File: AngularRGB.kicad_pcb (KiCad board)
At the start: 2 copper layers, 228.6 x 76.2 mm, 114 parts, among them SW1 SW_Push, SW1.25U1 MX_1.25U, SW1.25U2 MX_1.25U, SW1.25U3 MX_1.25U, SW1.25U4 MX_1.25U, SW1.25U5 MX_1.25U, SW1.25U6 MX_1.25U, SW1.75U1 MX_1.75U, SW1.75U2 MX_1.75U, SW10 MX_1U, SW11 MX_1U, SW12 MX_1U, SW13 MX_1U, SW14 MX_1U, SW15 MX_1U, SW16 MX_1U, SW17 MX_1U, SW18 MX_1U, SW19 MX_1U, SW2 MX_1U, SW2.25U1 MX_2.25U, SW2.75U1 MX_2.75U, SW20 MX_1U, SW21 MX_1U, SW22 MX_1U, SW23 MX_1U, SW24 MX_1U, SW25 MX_1U, SW26 MX_1U, SW27 MX_1U, SW28 MX_1U, SW29 MX_1U, SW3 MX_1U, SW30 MX_1U, SW31 MX_1U, SW32 MX_1U, SW33 MX_1U, SW4 MX_1U, SW5 MX_1U, SW6 MX_1U, SW7 MX_1U, SW8 MX_1U, SW9 MX_1U, U1 ATmega32U4-MU, U2 USB6B1, Y1 Crystal_GND24

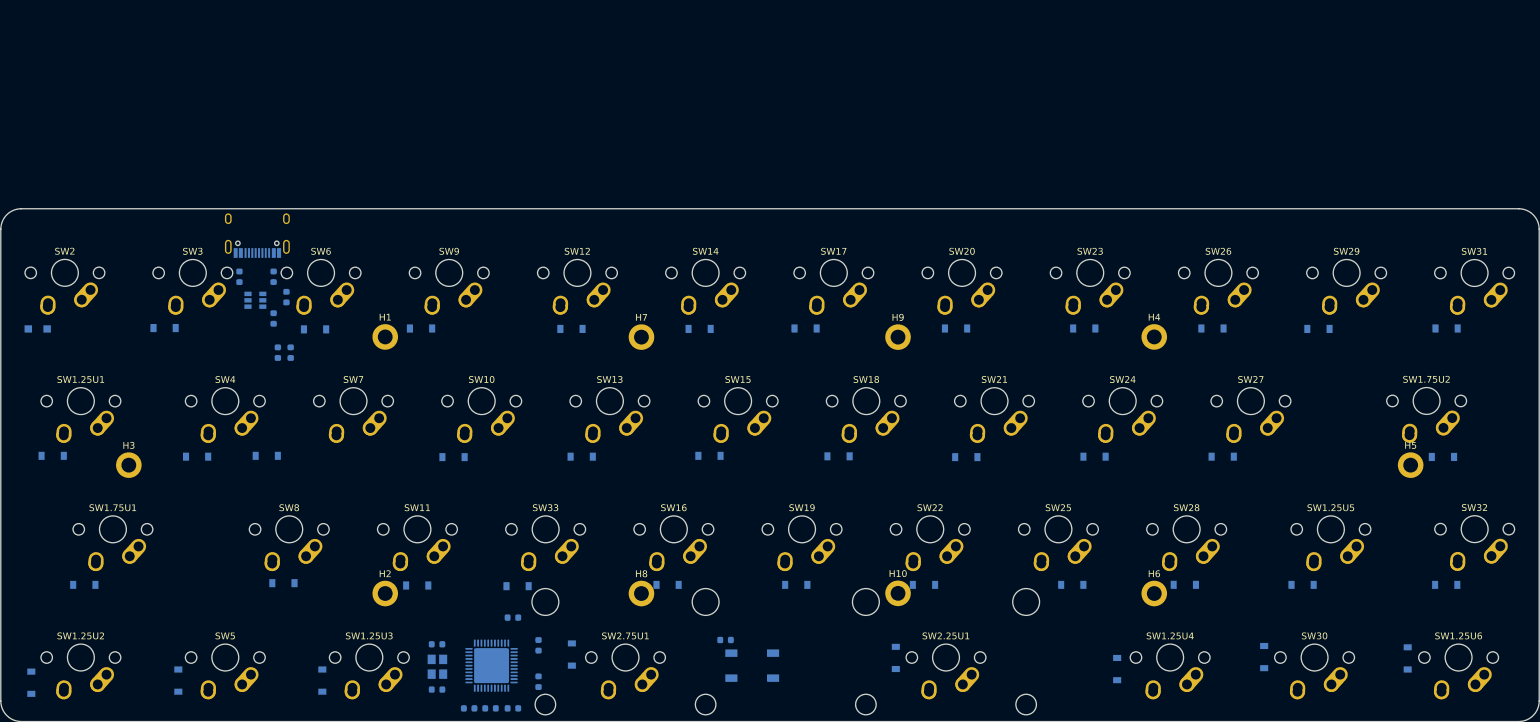
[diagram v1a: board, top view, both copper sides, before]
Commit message: LED Matrix Placement
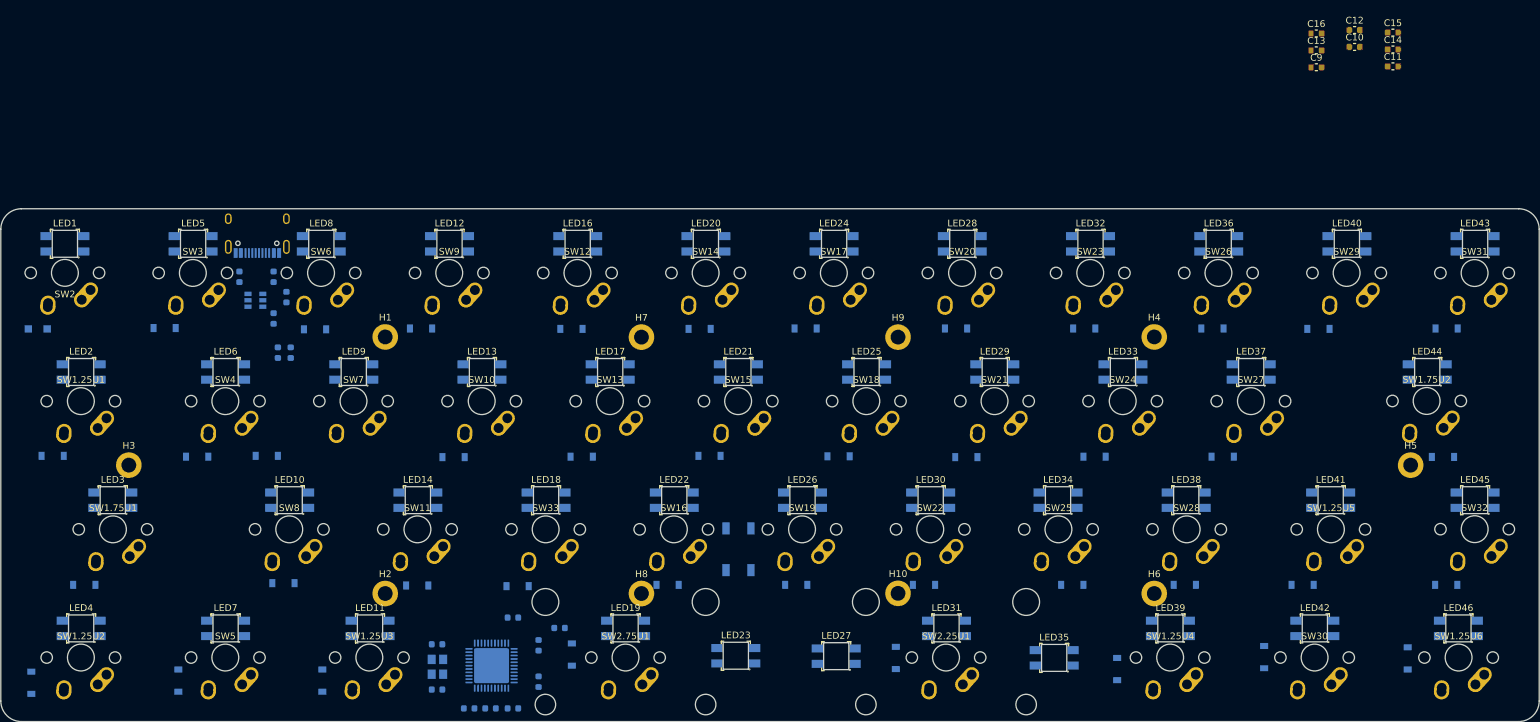
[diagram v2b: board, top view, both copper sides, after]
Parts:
- added C10: 100n, Capacitor_SMD:C_0603_1608Metric, F.Cu at (236.2, 30.0)
- added C11: 100n, Capacitor_SMD:C_0603_1608Metric, F.Cu at (241.9, 32.9)
- added C12: 100n, Capacitor_SMD:C_0603_1608Metric, F.Cu at (236.2, 27.5)
- added C13: 100n, Capacitor_SMD:C_0603_1608Metric, F.Cu at (230.5, 30.5)
- added C14: 100n, Capacitor_SMD:C_0603_1608Metric, F.Cu at (241.9, 30.4)
- added C15: 100n, Capacitor_SMD:C_0603_1608Metric, F.Cu at (241.9, 27.9)
- added C16: 100n, Capacitor_SMD:C_0603_1608Metric, F.Cu at (230.5, 28.0)
- added C9: 100n, Capacitor_SMD:C_0603_1608Metric, F.Cu at (230.5, 33.0)
- added LED1: WS2812, MX_Switches:REVERSE_LED, F.Cu at (44.6, 59.2)
- added LED10: WS2812, MX_Switches:REVERSE_LED, F.Cu at (78.0, 97.3)
- added LED11: WS2812, MX_Switches:REVERSE_LED, F.Cu at (89.9, 116.4)
- added LED12: WS2812, MX_Switches:REVERSE_LED, F.Cu at (101.7, 59.2)
- added LED13: WS2812, MX_Switches:REVERSE_LED, F.Cu at (106.5, 78.3)
- added LED14: WS2812, MX_Switches:REVERSE_LED, F.Cu at (97.0, 97.3)
- added LED16: WS2812, MX_Switches:REVERSE_LED, F.Cu at (120.8, 59.2)
- added LED17: WS2812, MX_Switches:REVERSE_LED, F.Cu at (125.6, 78.3)
- added LED18: WS2812, MX_Switches:REVERSE_LED, F.Cu at (116.1, 97.3)
- added LED19: WS2812, MX_Switches:REVERSE_LED, F.Cu at (127.9, 116.4)
- added LED2: WS2812, MX_Switches:REVERSE_LED, F.Cu at (47.0, 78.3)
- added LED20: WS2812, MX_Switches:REVERSE_LED, F.Cu at (139.8, 59.2)
- added LED21: WS2812, MX_Switches:REVERSE_LED, F.Cu at (144.6, 78.3)
- added LED22: WS2812, MX_Switches:REVERSE_LED, F.Cu at (135.1, 97.3)
- added LED23: WS2812, MX_Switches:REVERSE_LED, F.Cu at (144.2, 120.4)
- added LED24: WS2812, MX_Switches:REVERSE_LED, F.Cu at (158.9, 59.2)
- added LED25: WS2812, MX_Switches:REVERSE_LED, F.Cu at (163.7, 78.3)
- added LED26: WS2812, MX_Switches:REVERSE_LED, F.Cu at (154.2, 97.3)
- added LED27: WS2812, MX_Switches:REVERSE_LED, F.Cu at (159.2, 120.5)
- added LED28: WS2812, MX_Switches:REVERSE_LED, F.Cu at (177.9, 59.2)
- added LED29: WS2812, MX_Switches:REVERSE_LED, F.Cu at (182.7, 78.3)
- added LED3: WS2812, MX_Switches:REVERSE_LED, F.Cu at (51.7, 97.3)
- added LED30: WS2812, MX_Switches:REVERSE_LED, F.Cu at (173.2, 97.3)
- added LED31: WS2812, MX_Switches:REVERSE_LED, F.Cu at (175.6, 116.4)
- added LED32: WS2812, MX_Switches:REVERSE_LED, F.Cu at (197.0, 59.2)
- added LED33: WS2812, MX_Switches:REVERSE_LED, F.Cu at (201.8, 78.3)
- added LED34: WS2812, MX_Switches:REVERSE_LED, F.Cu at (192.1, 97.3)
- added LED35: WS2812, MX_Switches:REVERSE_LED, F.Cu at (191.6, 120.8)
- added LED36: WS2812, MX_Switches:REVERSE_LED, F.Cu at (216.0, 59.2)
- added LED37: WS2812, MX_Switches:REVERSE_LED, F.Cu at (220.8, 78.3)
- added LED38: WS2812, MX_Switches:REVERSE_LED, F.Cu at (211.2, 97.3)
- added LED39: WS2812, MX_Switches:REVERSE_LED, F.Cu at (208.8, 116.4)
- added LED4: WS2812, MX_Switches:REVERSE_LED, F.Cu at (47.0, 116.4)
- added LED40: WS2812, MX_Switches:REVERSE_LED, F.Cu at (235.1, 59.2)
- added LED41: WS2812, MX_Switches:REVERSE_LED, F.Cu at (232.6, 97.3)
- added LED42: WS2812, MX_Switches:REVERSE_LED, F.Cu at (230.3, 116.4)
- added LED43: WS2812, MX_Switches:REVERSE_LED, F.Cu at (254.1, 59.2)
- added LED44: WS2812, MX_Switches:REVERSE_LED, F.Cu at (247.0, 78.3)
- added LED45: WS2812, MX_Switches:REVERSE_LED, F.Cu at (254.1, 97.3)
- added LED46: WS2812, MX_Switches:REVERSE_LED, F.Cu at (251.6, 116.4)
- added LED5: WS2812, MX_Switches:REVERSE_LED, F.Cu at (63.6, 59.2)
- added LED6: WS2812, MX_Switches:REVERSE_LED, F.Cu at (68.4, 78.3)
- added LED7: WS2812, MX_Switches:REVERSE_LED, F.Cu at (68.4, 116.4)
- added LED8: WS2812, MX_Switches:REVERSE_LED, F.Cu at (82.7, 59.2)
- added LED9: WS2812, MX_Switches:REVERSE_LED, F.Cu at (87.5, 78.3)
- moved R1 24.7 mm to (118.1, 116.3)
- moved SW1 17.4 mm to (144.6, 104.6), turned to 90 degrees

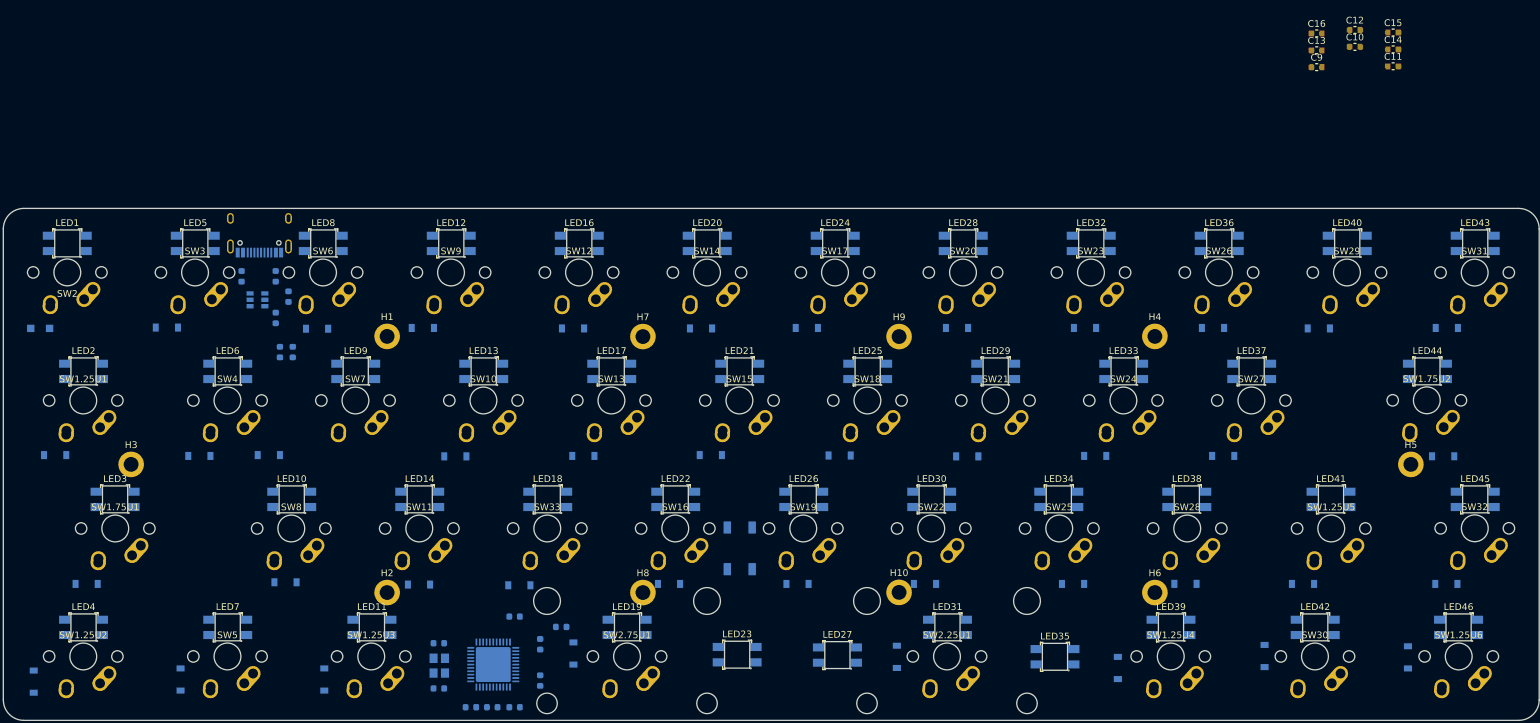
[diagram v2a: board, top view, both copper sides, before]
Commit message: LED Matrix Footprint swap
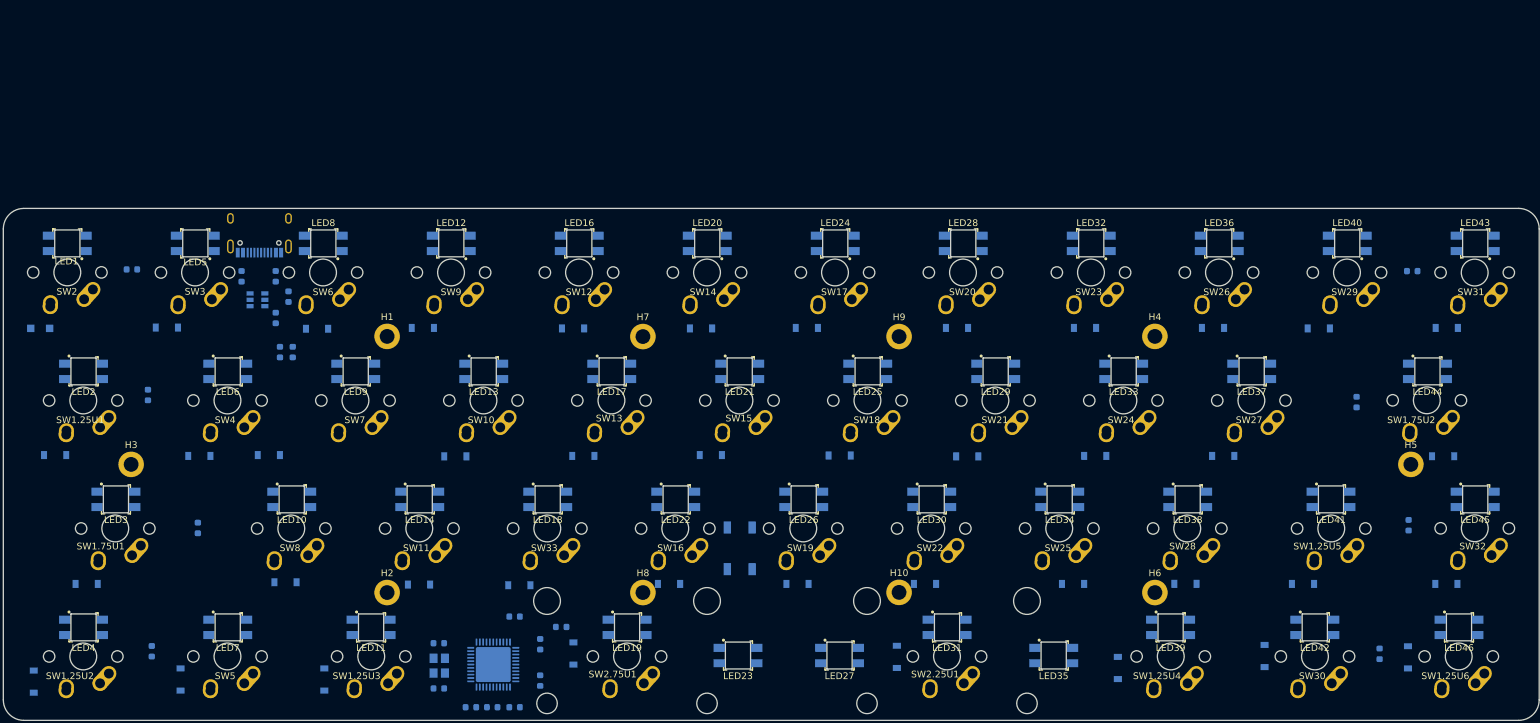
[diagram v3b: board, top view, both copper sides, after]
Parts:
- C10, C11, C12, C13, C14, C15, C16, C9: moved to B.Cu
- moved C16 196.3 mm to (57.1, 119.9), turned to 270 degrees
- moved C15 192.6 mm to (64.0, 101.6), turned to 270 degrees
- moved C11 191.7 mm to (56.6, 81.8), turned to 270 degrees
- moved C10 185.0 mm to (54.2, 63.1), turned to 180 degrees
- moved C13 90.3 mm to (239.9, 120.3), turned to 90 degrees
- moved C12 74.1 mm to (244.2, 101.2), turned to 270 degrees
- moved C14 52.8 mm to (236.4, 82.9), turned to 270 degrees
- moved C9 33.5 mm to (244.7, 63.4), turned to 180 degrees
- moved LED27 0.32 mm to (159.5, 120.6), turned to 180 degrees
- moved LED35 0.27 mm to (191.4, 120.6), turned to 180 degrees
- moved LED23 0.18 mm to (144.4, 120.6), turned to 180 degrees
- moved LED11 0.13 mm to (89.8, 116.4), turned to 180 degrees
- moved LED34 0.13 mm to (192.3, 97.3), turned to 180 degrees
- moved LED38 0.13 mm to (211.3, 97.3), turned to 180 degrees
- moved LED3 0.13 mm to (51.8, 97.3), turned to 180 degrees
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
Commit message: Matrix Connections
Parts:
- moved R1 30.9 mm to (143.5, 98.8)
- moved D34 15.8 mm to (216.7, 123.3)
- moved D9 3.81 mm to (78.4, 90.7)
- moved R5 1.75 mm to (78.0, 75.4)
- moved R6 1.68 mm to (76.4, 75.4)
- moved R4 0.66 mm to (74.9, 64.2)
- turned C5 to 0 degrees
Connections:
- net Net-(R5-Pad2) renamed /D_P
- net Net-(R6-Pad2) renamed /D_N
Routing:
- net R3: track 0.00 -> 211.3 mm
- net R2: track 0.00 -> 202.5 mm
- net R1: track 0.00 -> 200.0 mm
- net R0: track 0.00 -> 190.4 mm
- net /D-: track 0.00 -> 73.0 mm, vias 0 -> 2
- net /D+: track 0.00 -> 70.6 mm, vias 0 -> 2
- net C2: track 0.00 -> 64.1 mm, vias 0 -> 2
- net C4: track 0.00 -> 61.6 mm
- net C0: track 0.00 -> 61.2 mm
- net C11: track 0.00 -> 57.5 mm
- net C7: track 0.00 -> 57.1 mm
- net C9: track 0.00 -> 56.2 mm
- net C1: track 0.00 -> 53.2 mm
- net C10: track 0.00 -> 51.7 mm
- net C6: track 0.00 -> 45.2 mm
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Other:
- net class Power added: clearance 0.2, trace_width 0.4, via_dia 0.8, via_drill 0.4

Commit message: Finsihed Layout
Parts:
- added J1: Conn_01x09_Male, Connector_PinSocket_2.54mm:PinSocket_1x09_P2.54mm_Vertical, B.Cu at (37.3, 111.3)
- added TP1: TestPoint, TestPoint:TestPoint_Pad_D2.0mm, B.Cu at (92.2, 62.5)
- added TP2: TestPoint, TestPoint:TestPoint_Pad_D2.0mm, B.Cu at (92.2, 66.7)
- moved C15 4.99 mm to (59.7, 99.0), turned to 90 degrees
- moved D14 4.96 mm to (101.9, 109.9)
- moved C10 2.64 mm to (52.3, 61.2), turned to 270 degrees
- moved D4 1.84 mm to (41.4, 124.5), turned to 270 degrees
- moved C7 1.81 mm to (114.0, 117.3)
- moved D26 1.40 mm to (173.6, 109.9)
- moved D20 1.40 mm to (135.5, 109.9)
- moved C9 1.14 mm to (244.6, 62.2), turned to 270 degrees
- moved C14 0.87 mm to (236.2, 82.0), turned to 90 degrees
- moved R2 0.86 mm to (112.0, 114.8)
- moved C6 0.67 mm to (115.6, 124.1)
- moved C8 0.38 mm to (105.0, 128.3)
- moved C5 0.31 mm to (108.1, 128.3)
- turned C16 to 90 degrees
- turned LED1 to 180 degrees
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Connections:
- net Net-(U1-Pad18) renamed /SCL
- net Net-(U1-Pad19) renamed /SDA
- net Net-(U1-Pad8) renamed /SS
- U1 pad 1: Net-(U1-Pad1) -> /RST
- U1 pad 10: Net-(U1-Pad10) -> /MOSI
- U1 pad 11: Net-(U1-Pad11) -> /MISO
- U1 pad 12: Net-(U1-Pad12) -> R3
- U1 pad 20: Net-(U1-Pad20) -> R2
- U1 pad 21: Net-(U1-Pad21) -> R1
- U1 pad 22: Net-(U1-Pad22) -> R0
- U1 pad 25: Net-(U1-Pad25) -> C0
- U1 pad 26: Net-(U1-Pad26) -> C1
- U1 pad 27: Net-(U1-Pad27) -> C2
- U1 pad 28: Net-(U1-Pad28) -> C3
- U1 pad 29: Net-(U1-Pad29) -> /CS
- U1 pad 30: Net-(U1-Pad30) -> /IRQ
- U1 pad 31: Net-(U1-Pad31) -> C11
- U1 pad 32: Net-(U1-Pad32) -> C10
- U1 pad 36: Net-(U1-Pad36) -> C9
- U1 pad 37: Net-(U1-Pad37) -> C8
- U1 pad 38: Net-(U1-Pad38) -> C7
- U1 pad 39: Net-(U1-Pad39) -> C6
- U1 pad 40: Net-(U1-Pad40) -> C5
- U1 pad 41: Net-(U1-Pad41) -> C4
- U1 pad 9: Net-(U1-Pad9) -> /SCK
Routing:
- net VCC: track 23.7 -> 1298.9 mm, vias 0 -> 54
- net Net-(LED2-Pad4): track 0.00 -> 238.3 mm, vias 0 -> 2
- net Net-(LED4-Pad4): track 0.00 -> 238.1 mm, vias 0 -> 6
- net Net-(LED3-Pad4): track 0.00 -> 228.3 mm, vias 0 -> 2
- net C11: track 57.5 -> 219.0 mm, vias 0 -> 2
- net C10: track 51.7 -> 185.8 mm, vias 0 -> 2
- net /RST: track 0.00 -> 117.3 mm, vias 0 -> 2
- net C9: track 56.2 -> 172.0 mm, vias 0 -> 2
- net C8: track 43.3 -> 142.1 mm, vias 0 -> 2
- net /MOSI: track 0.00 -> 91.3 mm
- net /SCK: track 0.00 -> 86.6 mm, vias 0 -> 1
- net /MISO: track 0.00 -> 86.2 mm
- net /IRQ: track 0.00 -> 84.7 mm, vias 0 -> 3
- net /CS: track 0.00 -> 82.6 mm, vias 0 -> 3
- net C0: track 61.2 -> 139.6 mm, vias 0 -> 5
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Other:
- board text added: "CS"
- board text added: "GND"
- board text added: "IRQ"
- board text added: "MISO"
- board text added: "MOSI"
- board text added: "NC"
- board text added: "RST"
- board text added: "SCK"
- board text added: "VBUS"
- board text added: "VCC"

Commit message: Copper Pour
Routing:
- net GND: track 30.2 -> 112.0 mm, vias 0 -> 147
- net R0: track 254.9 -> 275.6 mm
- net VCC: track 1298.9 -> 1306.5 mm
- net Net-(D27-Pad2): track 0.00 -> 6.12 mm, vias 0 -> 1
- net Net-(D33-Pad2): track 0.00 -> 3.42 mm
- net Net-(R1-Pad2): track 75.9 -> 77.0 mm
- added copper zone on B.Cu, net GND
- added copper zone on F.Cu, net GND

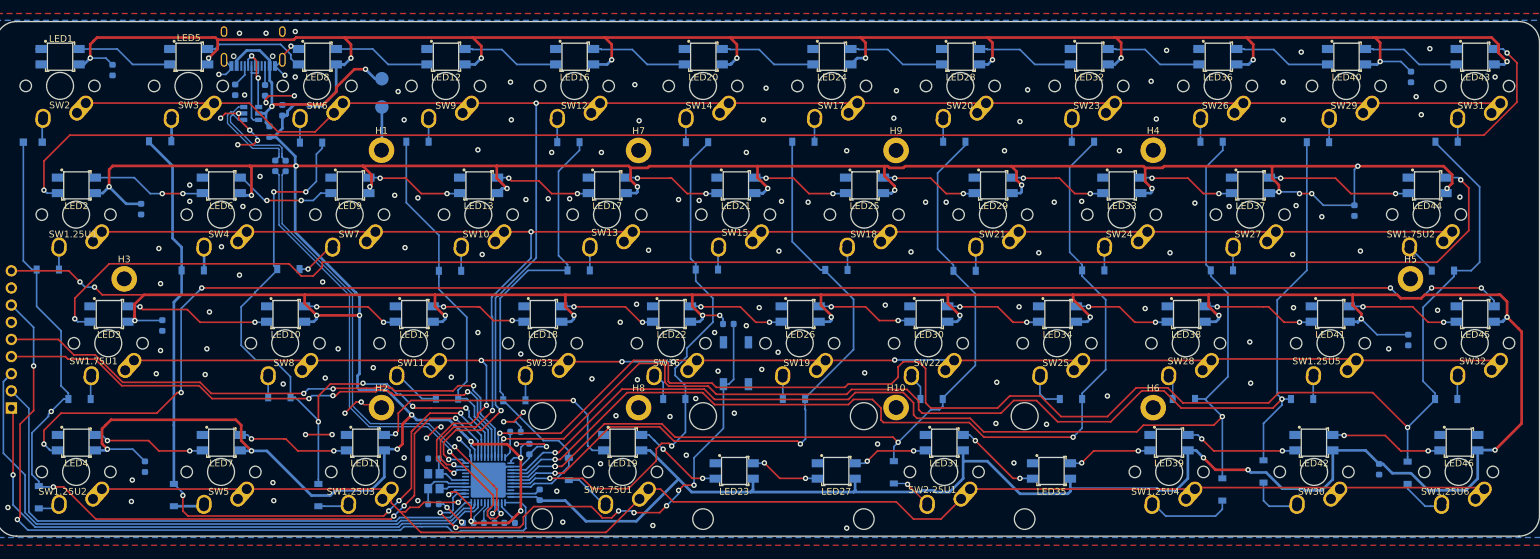
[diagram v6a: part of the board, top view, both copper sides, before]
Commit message: Fixed LED Input
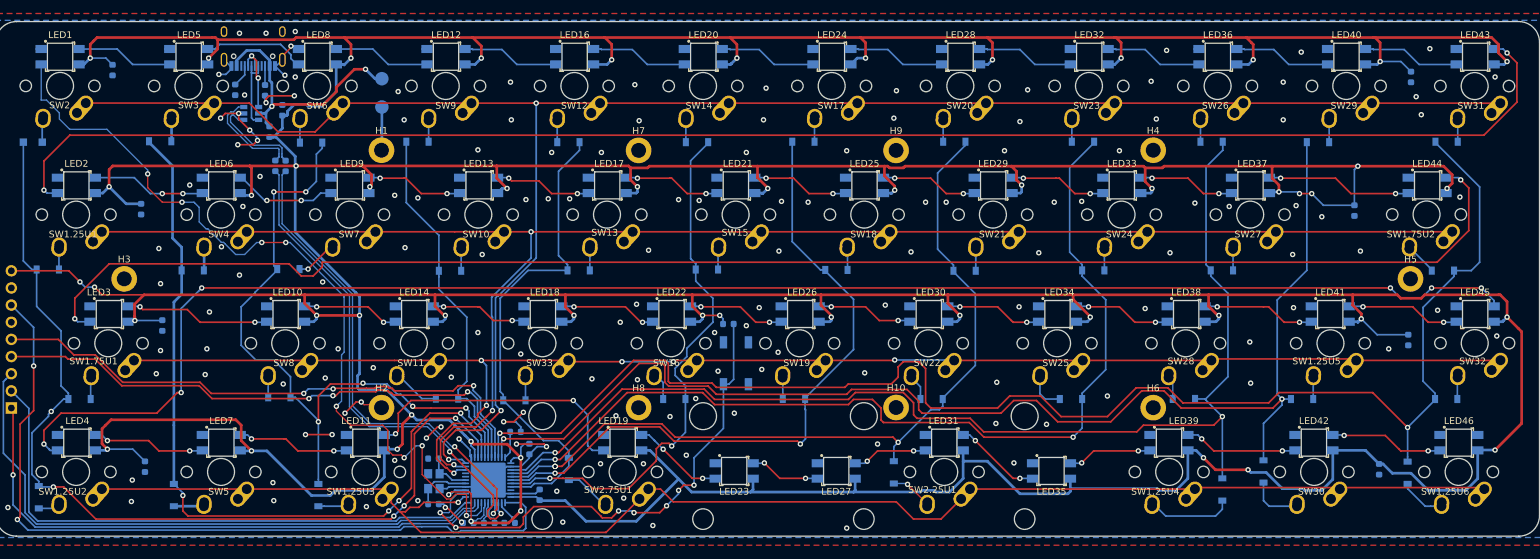
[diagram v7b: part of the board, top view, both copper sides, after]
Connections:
- U1 pad 8: /SS -> LED_INPUT
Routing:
- net LED_INPUT: track 0.00 -> 121.9 mm, vias 0 -> 8
- net VCC: track 1306.5 -> 1307.7 mm
- net Net-(R1-Pad2): track 77.0 -> 76.2 mm
- net GND: track 112.0 -> 111.7 mm, vias 147 -> 150
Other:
- net class Default: clearance 0.2 -> 0.153; trace_width 0.25 -> 0.2
- net class Power removed
- rule trace_clearance: 0.2 -> 0.153
- board text added: "AngularRGB"
- board text added: "Design by Henry Jiang"
- board text added: "Rev 1.0"
